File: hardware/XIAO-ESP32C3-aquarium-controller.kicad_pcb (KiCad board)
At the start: 2 copper layers, 72 x 99 mm, 44 parts, among them J1 Conn_01x02, J2 Conn_01x07, J3 Conn_01x06, J4 Conn_01x03, J5 Conn_01x03, K1 SANYOU_SRD_Form_C, K2 SANYOU_SRD_Form_C, K3 SANYOU_SRD_Form_C, Q1 AO3400A, Q2 AO3400A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

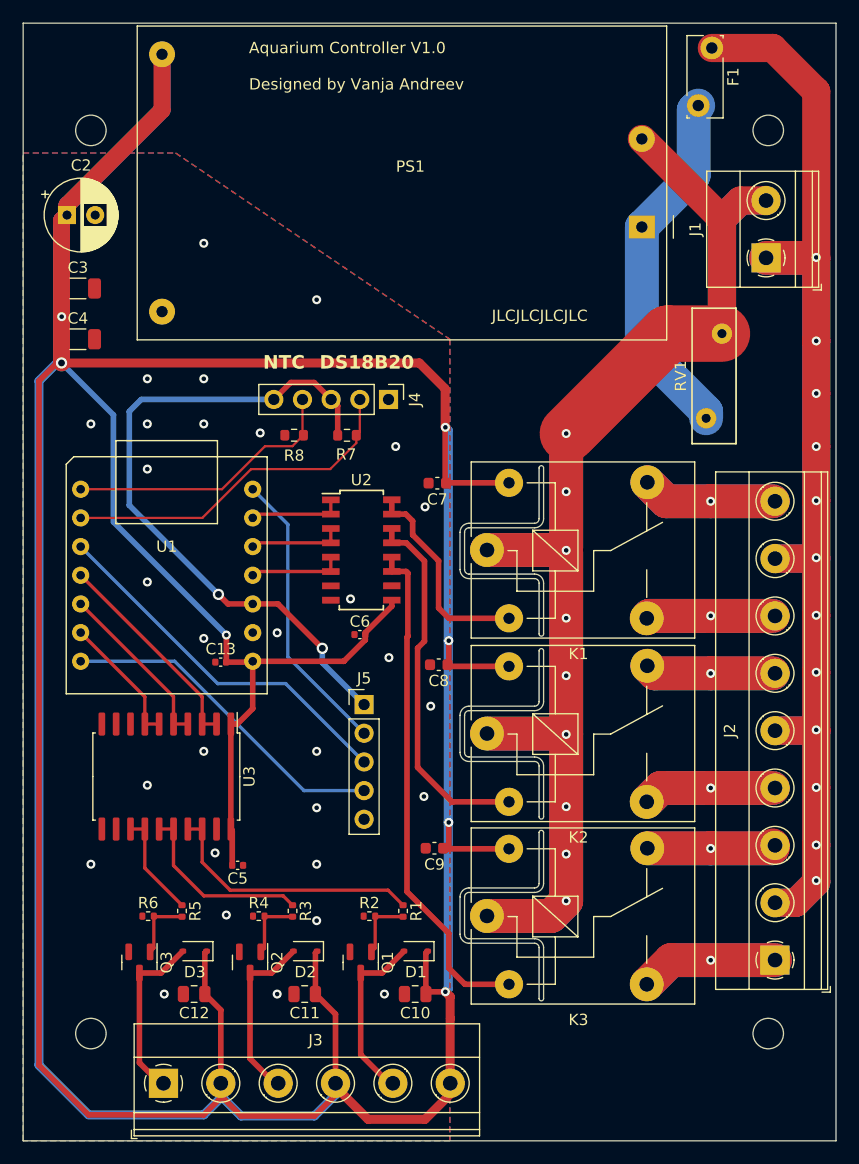
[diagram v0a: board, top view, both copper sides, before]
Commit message: change hole size
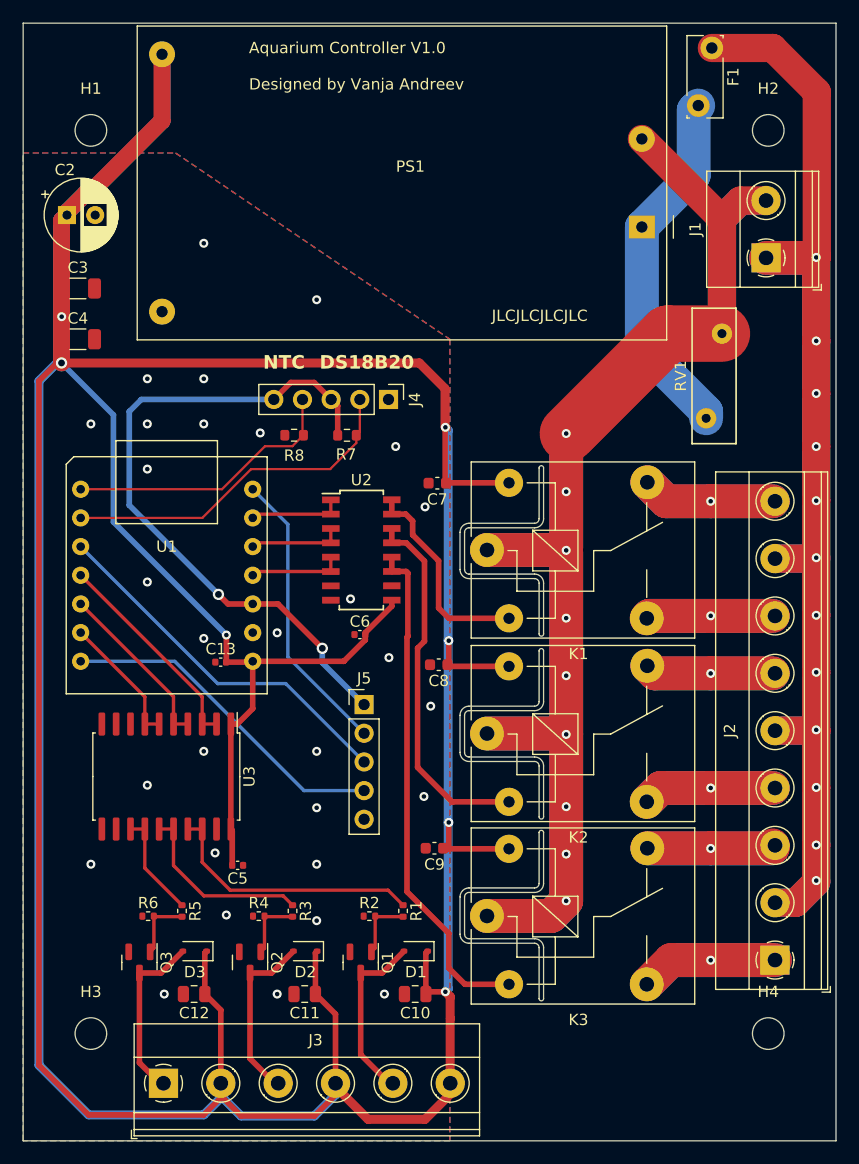
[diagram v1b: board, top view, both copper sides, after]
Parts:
- H1, H2, H3, H4: footprint MountingHole:MountingHole_2.7mm_M2.5 -> ProjectLibrary:MountingHole_2.8mm_M2.6

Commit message: labels
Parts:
- added kibuzzard-65101B66: G***, kibuzzard-65101B66, F.Cu at (57.2, 87.8)
- added kibuzzard-65101BA1: G***, kibuzzard-65101BA1, F.Cu at (57.2, 90.4)
- added kibuzzard-65101BBB: G***, kibuzzard-65101BBB, F.Cu at (57.2, 93.0)
- added kibuzzard-65101BCD: G***, kibuzzard-65101BCD, F.Cu at (57.2, 95.5)
- added kibuzzard-65101BE1: G***, kibuzzard-65101BE1, F.Cu at (57.2, 98.0)
- added kibuzzard-65101C3C: G***, kibuzzard-65101C3C, F.Cu at (49.1, 60.8)
- added kibuzzard-65101C61: G***, kibuzzard-65101C61, F.Cu at (68.0, 60.8)
- added kibuzzard-65101CEA: G***, kibuzzard-65101CEA, F.Cu at (52.8, 57.4)
- added kibuzzard-65101CEA: G***, kibuzzard-65101CEA, F.Cu at (57.9, 57.4)
- added kibuzzard-65101D0B: G***, kibuzzard-65101D0B, F.Cu at (55.4, 57.4)
- added kibuzzard-65101D31: G***, kibuzzard-65101D31, F.Cu at (60.5, 57.4)
- added kibuzzard-65101D45: G***, kibuzzard-65101D45, F.Cu at (63.0, 57.4)
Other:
- board text removed: "DS18B20"
- board text removed: "NTC"

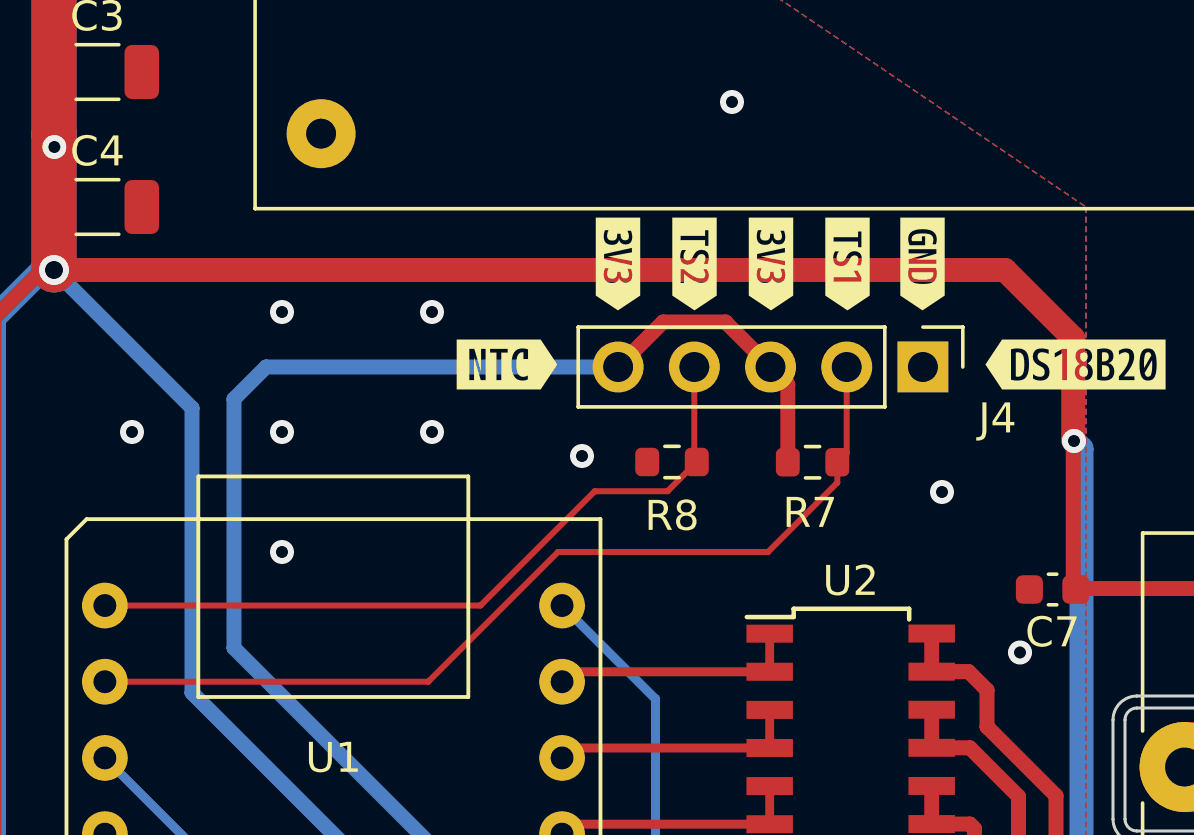
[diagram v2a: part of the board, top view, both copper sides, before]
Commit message: 5V/GND connector
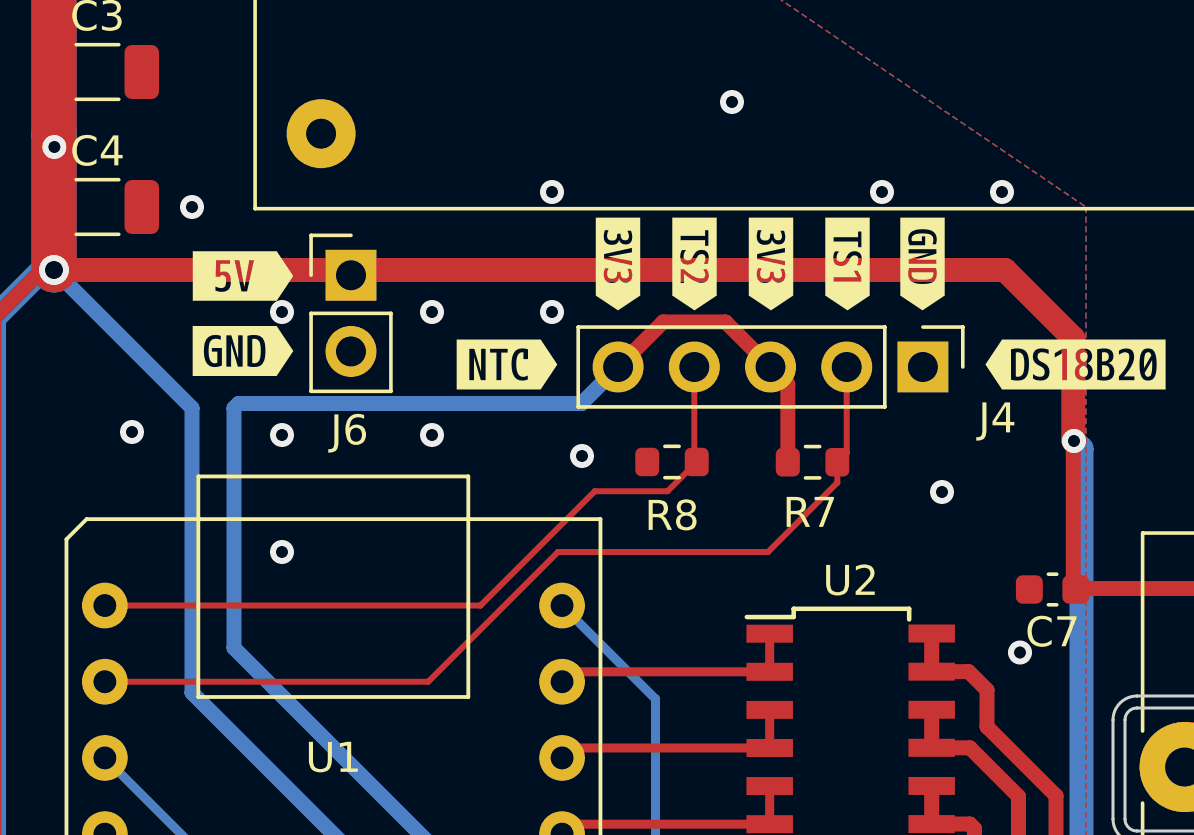
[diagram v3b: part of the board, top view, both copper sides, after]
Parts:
- added J6: Conn_01x02, Connector_PinHeader_2.54mm:PinHeader_1x02_P2.54mm_Vertical, F.Cu at (43.9, 57.8)
- added kibuzzard-65102A38: G***, kibuzzard-65102A38, F.Cu at (40.3, 57.8)
- added kibuzzard-65102A64: G***, kibuzzard-65102A64, F.Cu at (40.3, 60.3)
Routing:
- net GND: vias 30 -> 35

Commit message: some bom exclusions, jlcpcb rotations
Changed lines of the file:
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@@
     (attr board_only exclude_from_pos_files exclude_from_bom)
     (fp_text reference "kibuzzard-65102A64" (at 0 -3.881438) (layer "F.SilkS") hide
-        (effects (font (size 0 0)))
+        (effects (font (size 0 0) (thickness 0.15)))
     )
     (fp_text value "G***" (at 0 3.881438) (layer "F.SilkS") hide
-        (effects (font (size 0 0)))
+        (effects (font (size 0 0) (thickness 0.15)))
     )
     (fp_poly
@@
     (fp_line (start 1.6 0.8) (end -1.6 0.8)
       (stroke (width 0.1) (type solid)) (layer "F.Fab"))
-    (pad "1" smd roundrect (at -1.475 0) (size 1.15 1.8) (layers "F.Cu" "F.Paste" "F.Mask") (roundrect_rratio 0.217391)
+    (pad "1" smd roundrect (at -1.475 0) (size 1.15 1.8) (layers "F.Cu" "F.Paste" "F.Mask") (roundrect_rratio 0.2173913043)
       (net 1 "+5V") (pintype "passive"))
-    (pad "2" smd roundrect (at 1.475 0) (size 1.15 1.8) (layers "F.Cu" "F.Paste" "F.Mask") (roundrect_rratio 0.217391)
+    (pad "2" smd roundrect (at 1.475 0) (size 1.15 1.8) (layers "F.Cu" "F.Paste" "F.Mask") (roundrect_rratio 0.2173913043)
       (net 2 "GND") (pintype "passive"))
     (model "${KICAD6_3DMODEL_DIR}/Capacitor_SMD.3dshapes/C_1206_3216Metric.wrl"
@@
     (property "Sheetfile" "AC-DC.kicad_sch")
     (property "Sheetname" "AC-DC")
+    (property "exclude_from_bom" "")
     (property "ki_description" "Generic connector, single row, 01x02, script generated (kicad-library-utils/schlib/autogen/connector/)")
     (property "ki_keywords" "connector")
-    (attr through_hole)
+    (attr through_hole exclude_from_bom)
     (fp_text reference "J6" (at -0.05 5.175) (layer "F.SilkS")
         (effects (font (size 1 1) (thickness 0.15)))
@@
     (attr board_only exclude_from_pos_files exclude_from_bom)
     (fp_text reference "kibuzzard-65102A38" (at 0 -3.874294) (layer "F.SilkS") hide
-        (effects (font (size 0 0)))
+        (effects (font (size 0 0) (thickness 0.15)))
     )
     (fp_text value "G***" (at 0 3.874294) (layer "F.SilkS") hide
-        (effects (font (size 0 0)))
+        (effects (font (size 0 0) (thickness 0.15)))
     )
     (fp_poly

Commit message: text change
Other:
- board text added: "XIAO-ESP32C3 Aquarium Controller V1.0 Designed by Vanja Andreev"
- board text removed: "Aquarium Controller V1.0 Designed by Vanja Andreev"
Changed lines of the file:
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@@
   (gr_arc (start 76.700002 87.599999) (mid 76.465687 88.165684) (end 75.900002 88.399999)
     (stroke (width 0.1) (type default)) (layer "Edge.Cuts"))
-  (gr_text "Aquarium Controller V1.0\n\nDesigned by Vanja Andreev" (at 50.6 33.5) (layer "F.SilkS")
+  (gr_text "XIAO-ESP32C3 Aquarium Controller V1.0\n\nDesigned by Vanja Andreev" (at 50.6 33.5) (layer "F.SilkS")
     (effects (font (size 1 1) (thickness 0.15)) (justify left bottom))
   )

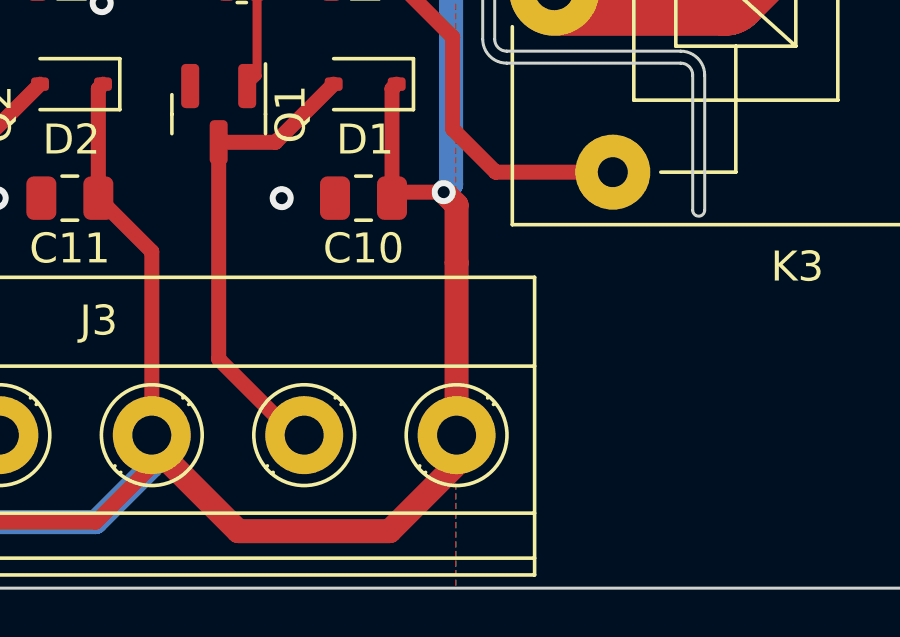
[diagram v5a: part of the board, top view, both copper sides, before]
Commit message: add aditional 5V track
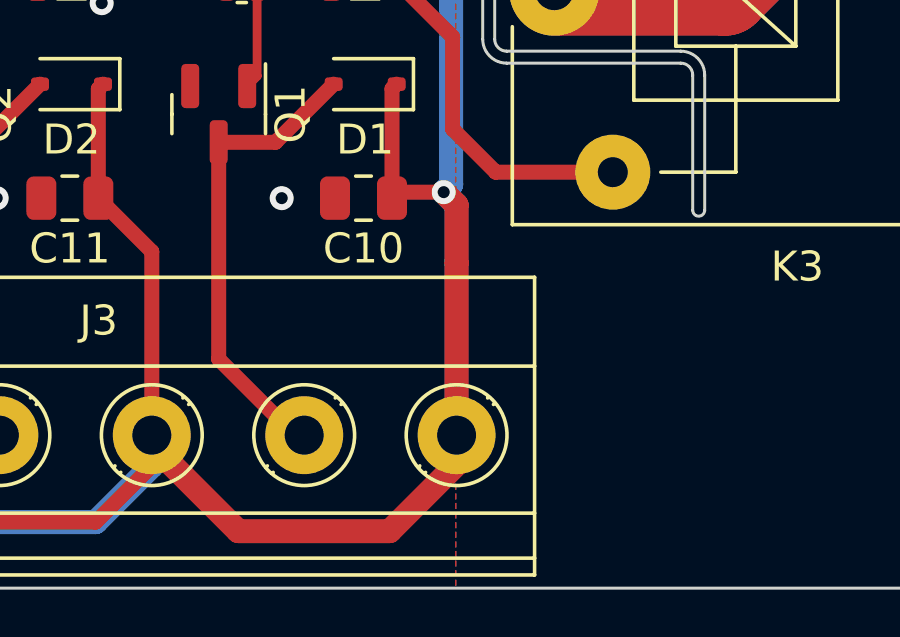
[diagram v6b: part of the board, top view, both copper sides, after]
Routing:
- net +5V: track 504.6 -> 513.2 mm
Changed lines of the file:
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@@
   (segment (start 34.013 53.086) (end 34 53.099) (width 1.5) (layer "B.Cu") (net 1))
   (segment (start 42.910939 30.24856) (end 42.910939 36.139061) (width 1.5) (layer "B.Cu") (net 1))
+  (segment (start 67.995 113.295) (end 68.425 113.725) (width 0.8) (layer "B.Cu") (net 1))
   (segment (start 68.3 82.2) (end 68.25 82.15) (width 0.8) (layer "B.Cu") (net 1))
   (segment (start 33.6 57.6) (end 32 59.2) (width 0.8) (layer "B.Cu") (net 1))
@@
   (segment (start 34 44.981621) (end 34 53.073) (width 1.5) (layer "B.Cu") (net 1))
   (segment (start 34.481621 44.5) (end 34 44.981621) (width 1.5) (layer "B.Cu") (net 1))
+  (segment (start 68.425 121.712) (end 68.425 115.648) (width 0.8) (layer "B.Cu") (net 1))
   (segment (start 48.11 122.51) (end 49.9 124.3) (width 0.8) (layer "B.Cu") (net 1))
   (segment (start 58.2685 121.717) (end 61.1515 124.6) (width 0.5) (layer "B.Cu") (net 1))
@@
   (segment (start 42.910939 36.139061) (end 36.5 42.55) (width 1.5) (layer "B.Cu") (net 1))
   (segment (start 38.6 62.2) (end 38.6 71.68875) (width 0.5) (layer "B.Cu") (net 1))
+  (segment (start 68.425 113.725) (end 68.425 115.648) (width 0.8) (layer "B.Cu") (net 1))
   (segment (start 68.25 98.35) (end 68.3 98.3) (width 0.8) (layer "B.Cu") (net 1))
   (segment (start 36.5 42.55) (end 36.173904 42.55) (width 1.5) (layer "B.Cu") (net 1))

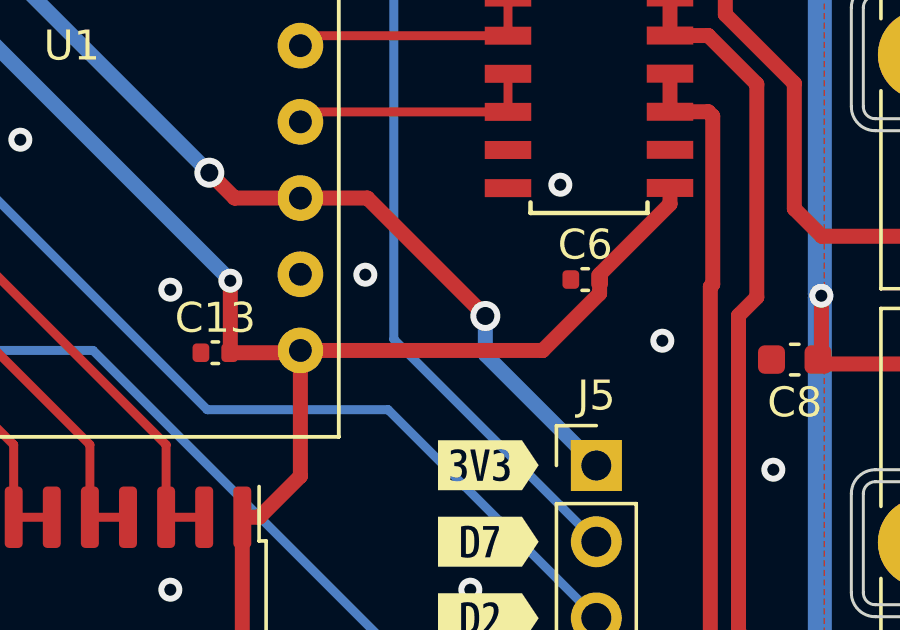
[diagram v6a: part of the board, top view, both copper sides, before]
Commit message: move some 5V track because of GND padding
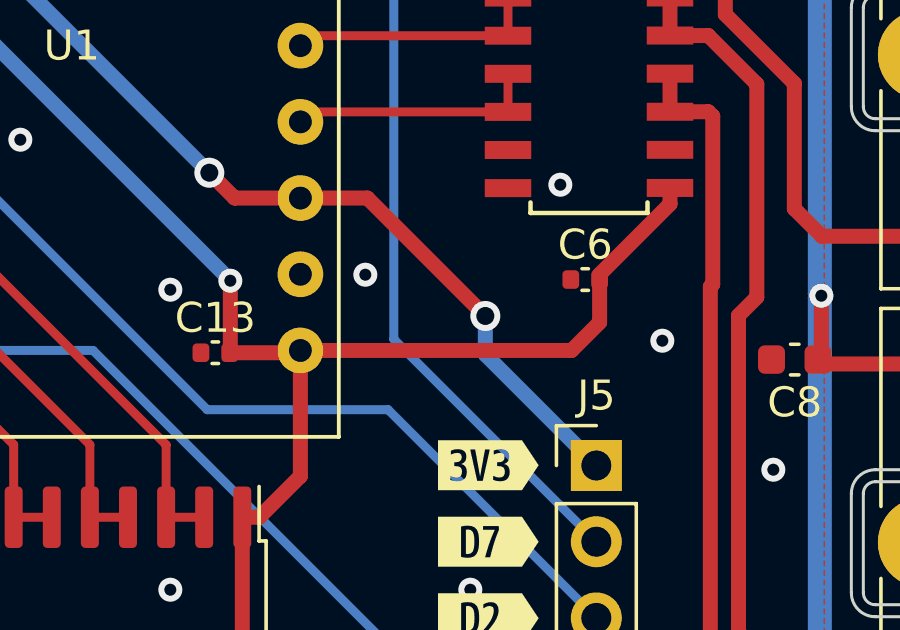
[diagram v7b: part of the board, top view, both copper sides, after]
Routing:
- net +5V: track 513.2 -> 513.7 mm
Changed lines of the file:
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@@
   (segment (start 50.93575 84.0245) (end 50.93575 88.21425) (width 0.5) (layer "F.Cu") (net 1))
   (segment (start 50.93575 88.21425) (end 49.566 89.584) (width 0.5) (layer "F.Cu") (net 1))
+  (segment (start 60.909 83.091) (end 60.909 81.661) (width 0.5) (layer "F.Cu") (net 1))
   (segment (start 66.477 113.3) (end 66.277 113.5) (width 0.5) (layer "F.Cu") (net 1))
   (segment (start 68.062 68.25) (end 67.975 68.163) (width 0.5) (layer "F.Cu") (net 1))
@@
   (segment (start 60.909 81.661) (end 60.909 81.491) (width 0.5) (layer "F.Cu") (net 1))
   (segment (start 68.094 68.218) (end 68.062 68.25) (width 0.5) (layer "F.Cu") (net 1))
-  (segment (start 60.909 82.128229) (end 60.909 81.661) (width 0.5) (layer "F.Cu") (net 1))
   (segment (start 68.43 113.73) (end 68.43 115.653) (width 0.8) (layer "F.Cu") (net 1))
   (segment (start 42.9035 30.256) (end 42.9035 36.1465) (width 1.5) (layer "F.Cu") (net 1))
@@
   (segment (start 68.3 84.217) (end 68.189 84.328) (width 0.5) (layer "F.Cu") (net 1))
   (segment (start 68.335 84.474) (end 68.189 84.328) (width 0.5) (layer "F.Cu") (net 1))
-  (segment (start 59.012729 84.0245) (end 60.909 82.128229) (width 0.5) (layer "F.Cu") (net 1))
   (segment (start 66.277 109.855) (end 66.432 109.7) (width 0.5) (layer "F.Cu") (net 1))
   (segment (start 33.6 57.6) (end 32 59.2) (width 0.5) (layer "F.Cu") (net 1))
@@
   (segment (start 73.637 68.218) (end 68.094 68.218) (width 0.5) (layer "F.Cu") (net 1))
   (segment locked (start 68.43 122.37) (end 68.43 121.717) (width 0.8) (layer "F.Cu") (net 1))
+  (segment (start 59.9755 84.0245) (end 60.909 83.091) (width 0.5) (layer "F.Cu") (net 1))
   (segment locked (start 58.27 122.43) (end 58.27 121.717) (width 0.5) (layer "F.Cu") (net 1))
   (segment (start 46.6 124.2) (end 48.11 122.69) (width 0.5) (layer "F.Cu") (net 1))
@@
   (segment (start 34 57.6) (end 33.6 57.6) (width 0.5) (layer "F.Cu") (net 1))
   (segment (start 42.9035 36.1465) (end 36.5 42.55) (width 1.5) (layer "F.Cu") (net 1))
+  (segment (start 50.93575 84.0245) (end 59.9755 84.0245) (width 0.5) (layer "F.Cu") (net 1))
   (segment (start 48.6 84.08) (end 48.58 84.1) (width 0.5) (layer "F.Cu") (net 1))
   (segment (start 68.3 100.634) (end 67.858 100.634) (width 0.5) (layer "F.Cu") (net 1))
@@
   (segment (start 65.7 57.6) (end 34 57.6) (width 0.8) (layer "F.Cu") (net 1))
   (segment (start 49.12 99.005) (end 48.999 98.884) (width 0.5) (layer "F.Cu") (net 1))
-  (segment (start 50.93575 84.0245) (end 59 84.0245) (width 0.5) (layer "F.Cu") (net 1))
   (segment (start 49.566 89.584) (end 48.999 89.584) (width 0.5) (layer "F.Cu") (net 1))
   (segment (start 63.256 79.144) (end 63.256 78.608) (width 0.5) (layer "F.Cu") (net 1))
   (segment locked (start 48.11 121.717) (end 48.11 122.51) (width 0.5) (layer "F.Cu") (net 1))
   (segment (start 34.481621 44.242283) (end 34.481621 44.5) (width 1.5) (layer "F.Cu") (net 1))
-  (segment (start 59 84.0245) (end 59.012729 84.0245) (width 0.5) (layer "F.Cu") (net 1))
   (segment (start 58.27 115.2818) (end 56.4882 113.5) (width 0.5) (layer "F.Cu") (net 1))
   (segment (start 68.3 98.3) (end 68.3 100.634) (width 0.5) (layer "F.Cu") (net 1))
